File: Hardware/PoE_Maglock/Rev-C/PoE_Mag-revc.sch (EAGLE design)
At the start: 81 parts, among them IC2 ATMEGA32U4-MU, J2 1X2-3.5MM, J3 1X2-3.5MM, J4 1X2-3.5MM, J5 1X2-3.5MM, J6 10103594-0001LF, Q1 35A/25V/8.5mΩ, Q3 35A/25V/8.5mΩ, Q5 35A/25V/8.5mΩ, Q6 35A/25V/8.5mΩ, SW1 SPST_TACT-KMR2, T1 DMG3415U, U2 SPX3819-3.3, U3 LMV358IDGKR, U4 W5500, U6 V_REG_317DPACK, X2 J1011FHANRUN, Y4 8MHz

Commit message: almost done with maglock, adjusted PoE tDocu footprint
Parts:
- removed C15, C16: 10uF, SparkFun-Passives:CAP0603-CAP
- removed U6: V_REG_317DPACK, SparkFun-IC-Power:V_REG_317DPACK
- added C14: 22nF, microbuilder:CAP_CERAMIC0603MINI
- added C4: 10µF 50V, microbuilder:CAP_CERAMIC0603MINI
- added J1, J10, J8, J9: (no value), SparkFun-Connectors:CONN_01
- added L1: 4.7uH, microbuilder:INDUCTORTDK_VLC5045
- added U$19: BUCK_CONVERTER, Heep:BUCK_CONVERTER
- C12, C13: value 0.1uF -> 22uF 10V; device microbuilder:CAP_CERAMIC0603_NO -> microbuilder:CAP_CERAMIC0603MINI
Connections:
- removed net 5: IC2.PC6(OC3A/!OC4A)
- removed net WIZ_RST_WIZ: R8.1, U4.RST_N
- new net N$14: C14.1, U$19.BST
- new net N$15: C14.2, L1.1, U$19.VSW
- net +3V3: now also R1.1, R2.1; no longer J7.2
- net +5V: now also C12.1, C13.1, J7.2, L1.2, U$19.FB; no longer C12.2, C16.1, U6.OUT
- net ACTLED: now also X2.YEL-C; no longer X2.YEL-A
- net EN1: now also IC2.PC6(OC3A/!OC4A), J1.1; no longer IC2.PB6(OC1B/OC4B/ADC13)
- net EN2: now also IC2.PB6(OC1B/OC4B/ADC13), J8.1; no longer IC2.PB5(OC1A/ADC12/!OC4B)
- net EN3: now also IC2.PB5(OC1A/ADC12/!OC4B), J9.1; no longer IC2.PD7(OC4D/ADC10/T0)
- net EN4: now also IC2.PD7(OC4D/ADC10/T0), J10.1; no longer IC2.PD6(T1/ADC9/!OC4D)
- net GND: now also C12.2, C4.2, U$19.GND, U$19.PGND; no longer C12.1, C15.2, C16.2, R1.1, R2.1, U6.ADJ
- net LNKLED: now also X2.GRN-C; no longer X2.GRN-A
- net N$3: now also X2.GRN-A; no longer X2.GRN-C
- net N$4: now also X2.YEL-A; no longer X2.YEL-C
- net VBAT: now also C4.1, U$19.VCC; no longer C13.1, C15.1, U6.IN
- net WIZ_RST: now also R8.1, U4.RST_N
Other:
- moved on the sheet: C12, C13, R1, R2

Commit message: ready for dylan review
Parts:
- added J11, J12: (no value), SparkFun-Connectors:CONN_04
- added J13: (no value), SparkFun-Connectors:CONN_041X04_NO_SILK
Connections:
- net +3V3: now also J12.1, J12.2, J12.3, J12.4
- net A0: now also J13.4
- net A1: now also J13.3
- net A2: now also J13.2
- net A3: now also J13.1
- net GND: now also J11.1, J11.2, J11.3, J11.4
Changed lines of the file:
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@@
 <part name="J9" library="SparkFun-Connectors" deviceset="CONN_01" device=""/>
 <part name="J10" library="SparkFun-Connectors" deviceset="CONN_01" device=""/>
+<part name="J11" library="SparkFun-Connectors" deviceset="CONN_04" device=""/>
+<part name="J12" library="SparkFun-Connectors" deviceset="CONN_04" device=""/>
+<part name="J13" library="SparkFun-Connectors" deviceset="CONN_04" device="1X04_NO_SILK"/>
+<part name="GND10" library="supply1" deviceset="GND" device=""/>
+<part name="+3V13" library="supply1" deviceset="+3V3" device=""/>
 </parts>
 <sheets>
@@
 <instance part="J9" gate="G$1" x="276.86" y="149.86"/>
 <instance part="J10" gate="G$1" x="276.86" y="134.62"/>
+<instance part="J11" gate="G$1" x="375.92" y="45.72" rot="R180"/>
+<instance part="J12" gate="G$1" x="375.92" y="25.4" rot="R180"/>
+<instance part="J13" gate="G$1" x="327.66" y="48.26" rot="R180"/>
+<instance part="GND10" gate="1" x="370.84" y="38.1"/>
+<instance part="+3V13" gate="G$1" x="370.84" y="17.78" rot="R180"/>
 </instances>
 <busses>
@@
 <pinref part="U$25" gate="G$1" pin="GND"/>
 </segment>
+<segment>
+<pinref part="J11" gate="G$1" pin="4"/>
+<pinref part="GND10" gate="1" pin="GND"/>
+<pinref part="J11" gate="G$1" pin="3"/>
+<wire x1="370.84" y1="40.64" x2="370.84" y2="43.18" width="0.1524" layer="91"/>
+<junction x="370.84" y="40.64"/>
+<pinref part="J11" gate="G$1" pin="2"/>
+<wire x1="370.84" y1="43.18" x2="370.84" y2="45.72" width="0.1524" layer="91"/>
+<junction x="370.84" y="43.18"/>
+<pinref part="J11" gate="G$1" pin="1"/>
+<wire x1="370.84" y1="45.72" x2="370.84" y2="48.26" width="0.1524" layer="91"/>
+<junction x="370.84" y="45.72"/>
+</segment>
 </net>
 <net name="RD-" class="0">
@@
 <label x="292.1" y="327.66" size="1.778" layer="95"/>
 </segment>
+<segment>
+<pinref part="J13" gate="G$1" pin="1"/>
+<wire x1="322.58" y1="50.8" x2="312.42" y2="50.8" width="0.1524" layer="91"/>
+<label x="312.42" y="50.8" size="1.778" layer="95"/>
+</segment>
 </net>
 <net name="A2" class="0">
@@
 <label x="292.1" y="325.12" size="1.778" layer="95"/>
 </segment>
+<segment>
+<pinref part="J13" gate="G$1" pin="2"/>
+<wire x1="322.58" y1="48.26" x2="312.42" y2="48.26" width="0.1524" layer="91"/>
+<label x="312.42" y="48.26" size="1.778" layer="95"/>
+</segment>
 </net>
 <net name="A1" class="0">
@@
 <pinref part="IC2" gate="G$1" pin="PF6(ADC6/TDO)"/>
 <label x="292.1" y="322.58" size="1.778" layer="95"/>
+</segment>
+<segment>
+<pinref part="J13" gate="G$1" pin="3"/>
+<wire x1="322.58" y1="45.72" x2="312.42" y2="45.72" width="0.1524" layer="91"/>
+<label x="312.42" y="45.72" size="1.778" layer="95"/>
 </segment>
 </net>
@@
 <pinref part="+3V5" gate="G$1" pin="+3V3"/>
 </segment>
+<segment>
+<pinref part="J12" gate="G$1" pin="4"/>
+<pinref part="+3V13" gate="G$1" pin="+3V3"/>
+<pinref part="J12" gate="G$1" pin="1"/>
+<pinref part="J12" gate="G$1" pin="2"/>
+<wire x1="370.84" y1="27.94" x2="370.84" y2="25.4" width="0.1524" layer="91"/>
+<pinref part="J12" gate="G$1" pin="3"/>
+<wire x1="370.84" y1="25.4" x2="370.84" y2="22.86" width="0.1524" layer="91"/>
+<junction x="370.84" y="25.4"/>
+<wire x1="370.84" y1="22.86" x2="370.84" y2="20.32" width="0.1524" layer="91"/>
+<junction x="370.84" y="22.86"/>
+<junction x="370.84" y="20.32"/>
+</segment>
 </net>
 <net name="VBUS" class="0">
@@
 <label x="292.1" y="320.04" size="1.778" layer="95"/>
 </segment>
-</net>
+<segment>
+<wire x1="322.58" y1="43.18" x2="312.42" y2="43.18" width="0.1524" layer="91"/>
+<label x="312.42" y="43.18" size="1.778" layer="95"/>
+<pinref part="J13" gate="G$1" pin="4"/>
+</segment>
+</net>

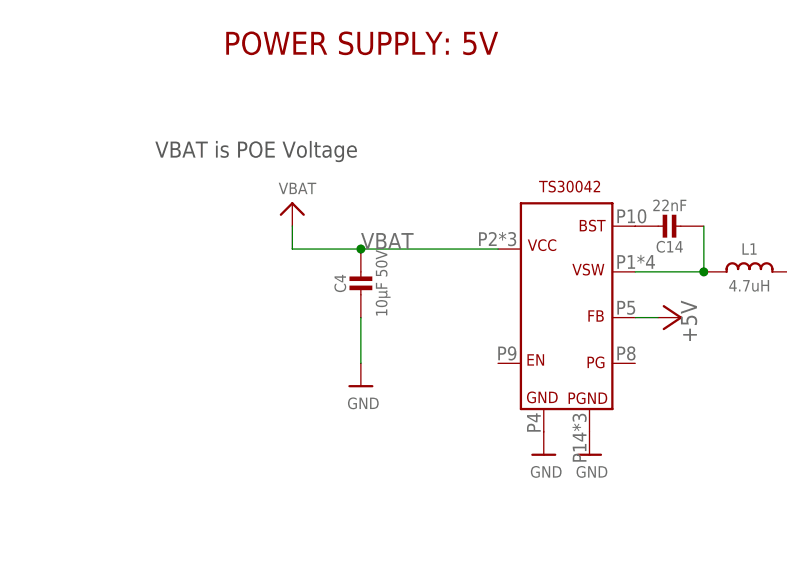
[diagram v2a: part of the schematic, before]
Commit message: HEEP-651 updated capacitor voltage ratings to reflect true minimum requirements
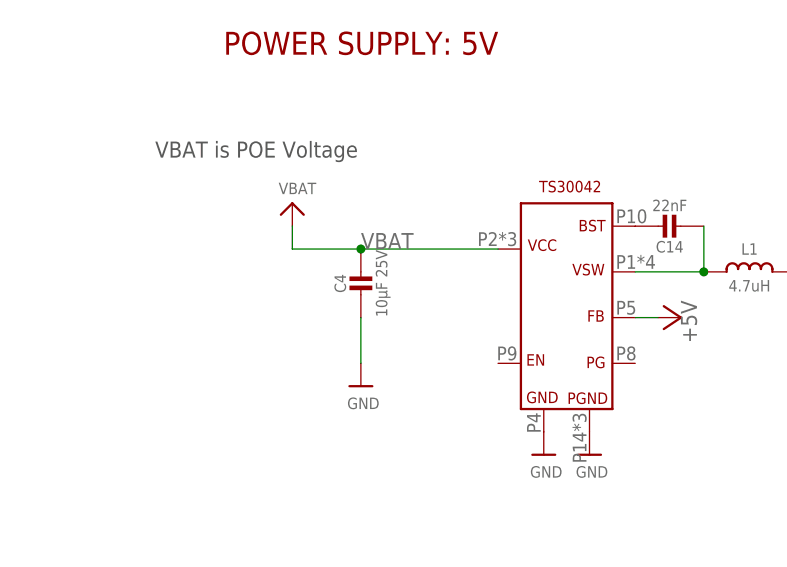
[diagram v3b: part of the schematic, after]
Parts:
- C4: value 10µF 50V -> 10µF 25V
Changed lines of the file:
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@@
 <part name="P+2" library="supply1" deviceset="+5V" device=""/>
 <part name="U$19" library="Heep" deviceset="BUCK_CONVERTER" device=""/>
-<part name="C4" library="microbuilder" deviceset="CAP_CERAMIC" device="0603MINI" value="10µF 50V"/>
+<part name="C4" library="microbuilder" deviceset="CAP_CERAMIC" device="0603MINI" value="10µF 25V"/>
 <part name="U$20" library="microbuilder" deviceset="GND" device=""/>
 <part name="U$22" library="microbuilder" deviceset="GND" device=""/>
